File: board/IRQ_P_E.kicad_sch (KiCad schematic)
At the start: 21 parts, among them IC5 74LS219, IC6 74LS219, IC7 74LS219, IC8 74LS219, U13 74F08, U42 74F157, U43 74F157, U44 74LS148, U45 74LS148, U46 74F32

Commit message: Board V1.1G
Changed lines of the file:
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@@
 (kicad_sch
-	(version 20231120)
+	(version 20250114)
 	(generator "eeschema")
-	(generator_version "8.0")
+	(generator_version "9.0")
 	(paper "USLetter")
 	(title_block
 		(title "IRQ Priority Logic and Vector Memory")
 		(date "2025-03-04")
-		(rev "1.0F")
+		(rev "1.1A")
 		(company "Data Tuning")
 		(comment 1 "Hydra 16")
@@
 	(wire
 		(pts
-			(xy 181.61 33.02) (xy 195.58 33.02)
-		)
-		(stroke
-			(width 0)
-			(type default)
-		)
-	)
-	(wire
-		(pts
 			(xy 38.1 36.83) (xy 39.37 36.83)
 		)
@@
 	(wire
 		(pts
+			(xy 190.5 60.96) (xy 198.12 60.96)
+		)
+		(stroke
+			(width 0)
+			(type default)
+		)
+	)
+	(wire
+		(pts
 			(xy 36.83 153.67) (xy 36.83 175.26)
 		)
@@
 	(wire
 		(pts
-			(xy 195.58 33.02) (xy 195.58 60.96)
-		)
-		(stroke
-			(width 0)
-			(type default)
-		)
-	)
-	(wire
-		(pts
 			(xy 243.84 123.19) (xy 241.3 123.19)
 		)
@@
 	(wire
 		(pts
+			(xy 190.5 33.02) (xy 190.5 60.96)
+		)
+		(stroke
+			(width 0)
+			(type default)
+		)
+	)
+	(wire
+		(pts
 			(xy 191.77 118.11) (xy 186.69 118.11)
 		)
@@
 	(wire
 		(pts
-			(xy 153.67 27.94) (xy 184.15 27.94)
+			(xy 153.67 22.86) (xy 203.2 22.86)
 		)
 		(stroke
@@
 		)
 	)
+	(wire
+		(pts
+			(xy 181.61 33.02) (xy 190.5 33.02)
+		)
+		(stroke
+			(width 0)
+			(type default)
+		)
+	)
 	(bus
 		(pts
@@
 	(wire
 		(pts
+			(xy 153.67 22.86) (xy 153.67 27.94)
+		)
+		(stroke
+			(width 0)
+			(type default)
+		)
+	)
+	(wire
+		(pts
 			(xy 118.11 34.29) (xy 123.19 34.29)
 		)
@@
 	(wire
 		(pts
-			(xy 195.58 60.96) (xy 198.12 60.96)
-		)
-		(stroke
-			(width 0)
-			(type default)
-		)
-	)
-	(wire
-		(pts
 			(xy 227.33 135.89) (xy 227.33 165.1)
 		)
@@
 	(label "D3"
 		(at 76.2 139.7 0)
-		(fields_autoplaced yes)
 		(effects
 			(font
@@
 	(label "D7"
 		(at 77.47 157.48 0)
-		(fields_autoplaced yes)
 		(effects
 			(font
@@
 	(label "D2"
 		(at 77.47 144.78 0)
-		(fields_autoplaced yes)
 		(effects
 			(font
@@
 	(label "D3"
 		(at 151.13 139.7 0)
-		(fields_autoplaced yes)
 		(effects
 			(font
@@
 	(label "D5"
 		(at 36.83 157.48 0)
-		(fields_autoplaced yes)
 		(effects
 			(font
@@
 	(label "D4"
 		(at 101.6 157.48 0)
-		(fields_autoplaced yes)
 		(effects
 			(font
@@
 	(label "V3"
 		(at 195.58 104.14 0)
-		(fields_autoplaced yes)
 		(effects
 			(font
@@
 	(label "D7"
 		(at 152.4 157.48 0)
-		(fields_autoplaced yes)
 		(effects
 			(font
@@
 	(label "V0"
 		(at 195.58 73.66 0)
-		(fields_autoplaced yes)
 		(effects
 			(font
@@
 	(label "V1"
 		(at 195.58 83.82 0)
-		(fields_autoplaced yes)
 		(effects
 			(font
@@
 	(label "D1"
 		(at 106.68 142.24 0)
-		(fields_autoplaced yes)
 		(effects
 			(font
@@
 	(label "D0"
 		(at 36.83 137.16 0)
-		(fields_autoplaced yes)
 		(effects
 			(font
@@
 	(label "D4"
 		(at 33.02 157.48 0)
-		(fields_autoplaced yes)
 		(effects
 			(font
@@
 	(label "D6"
 		(at 148.59 157.48 0)
-		(fields_autoplaced yes)
 		(effects
 			(font
@@
 	(label "D5"
 		(at 105.41 157.48 0)
-		(fields_autoplaced yes)
 		(effects
 			(font
@@
 	(label "D0"
 		(at 105.41 137.16 0)
-		(fields_autoplaced yes)
 		(effects
 			(font
@@
 	(label "V2"
 		(at 195.58 93.98 0)
-		(fields_autoplaced yes)
 		(effects
 			(font
@@
 	(label "D6"
 		(at 73.66 157.48 0)
-		(fields_autoplaced yes)
 		(effects
 			(font
@@
 	(label "D1"
 		(at 38.1 142.24 0)
-		(fields_autoplaced yes)
 		(effects
 			(font
@@
 	(label "D2"
 		(at 152.4 144.78 0)
-		(fields_autoplaced yes)
 		(effects
 			(font
@@
 	(global_label "IRQB"
 		(shape output)
-		(at 184.15 27.94 0)
+		(at 203.2 22.86 0)
 		(fields_autoplaced yes)
 		(effects
@@
 		)
 		(property "Intersheetrefs" "${INTERSHEET_REFS}"
-			(at 191.6105 27.94 0)
+			(at 210.6605 22.86 0)
 			(effects
 				(font
@@
 		(dnp no)
 		(property "Reference" "U46"
-			(at 173.99 24.13 0)
+			(at 174.752 25.146 0)
 			(effects
 				(font
@@
 		)
 		(property "Value" "74F32"
-			(at 173.99 26.67 0)
+			(at 174.752 27.686 0)
 			(effects
 				(font

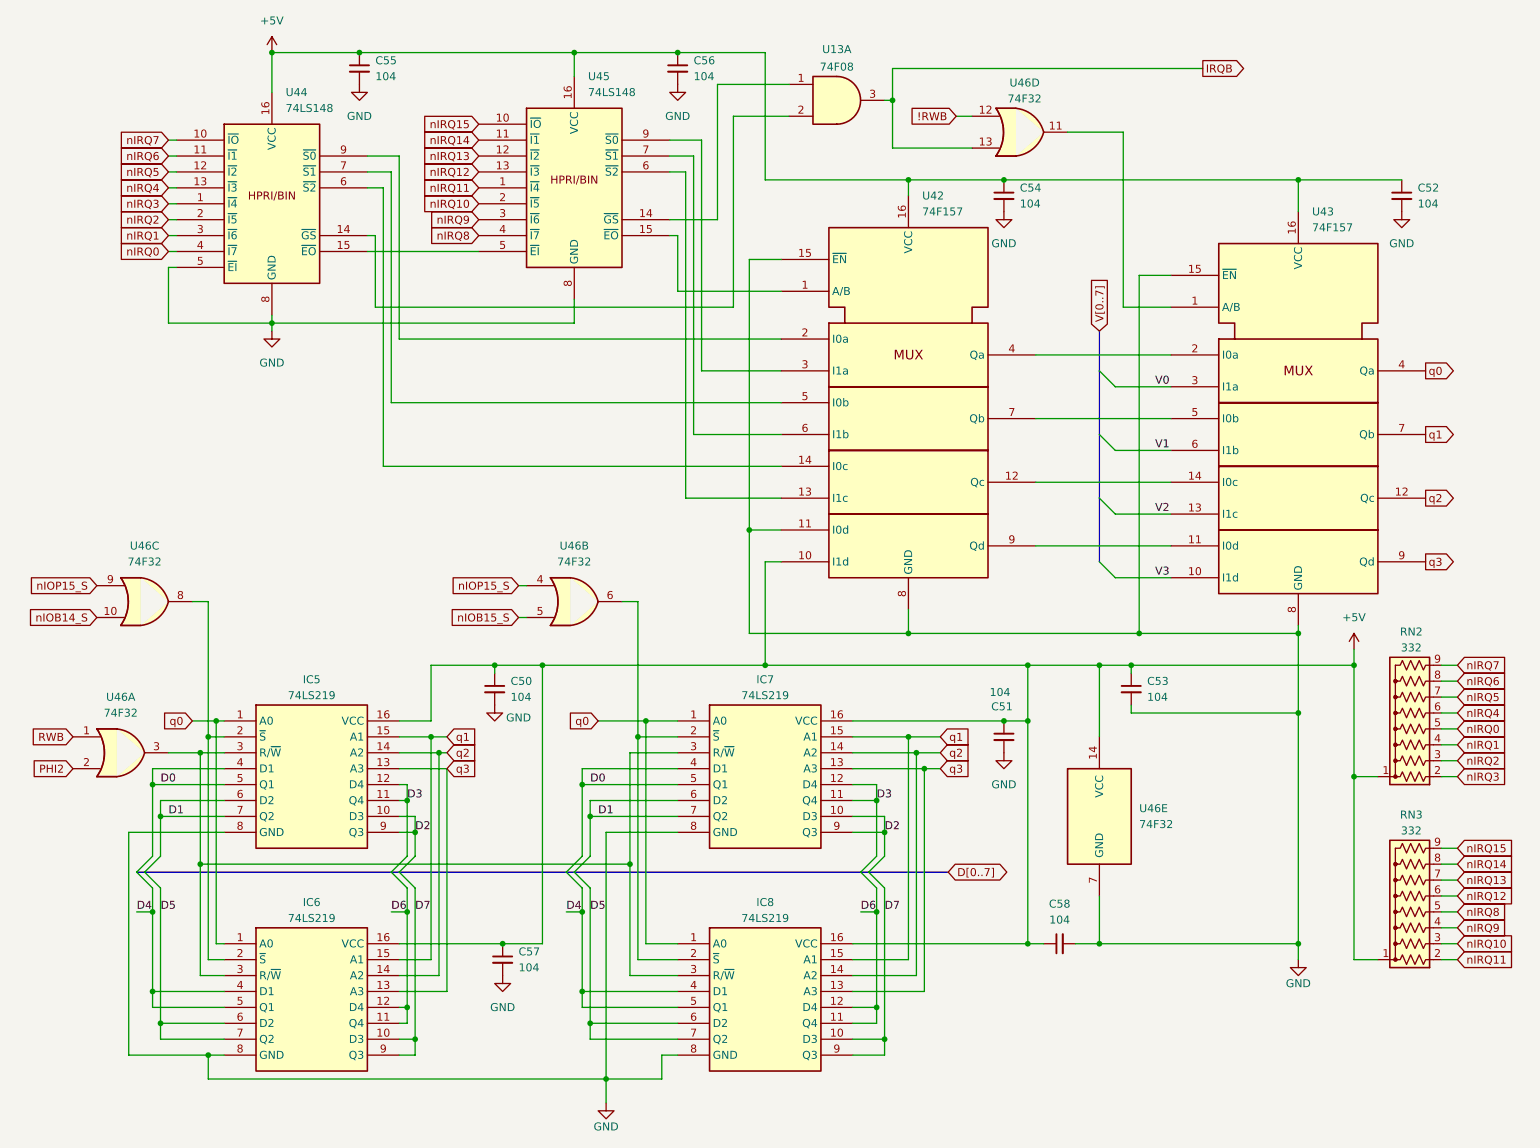
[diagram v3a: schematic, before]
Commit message: V1.3C without board traces
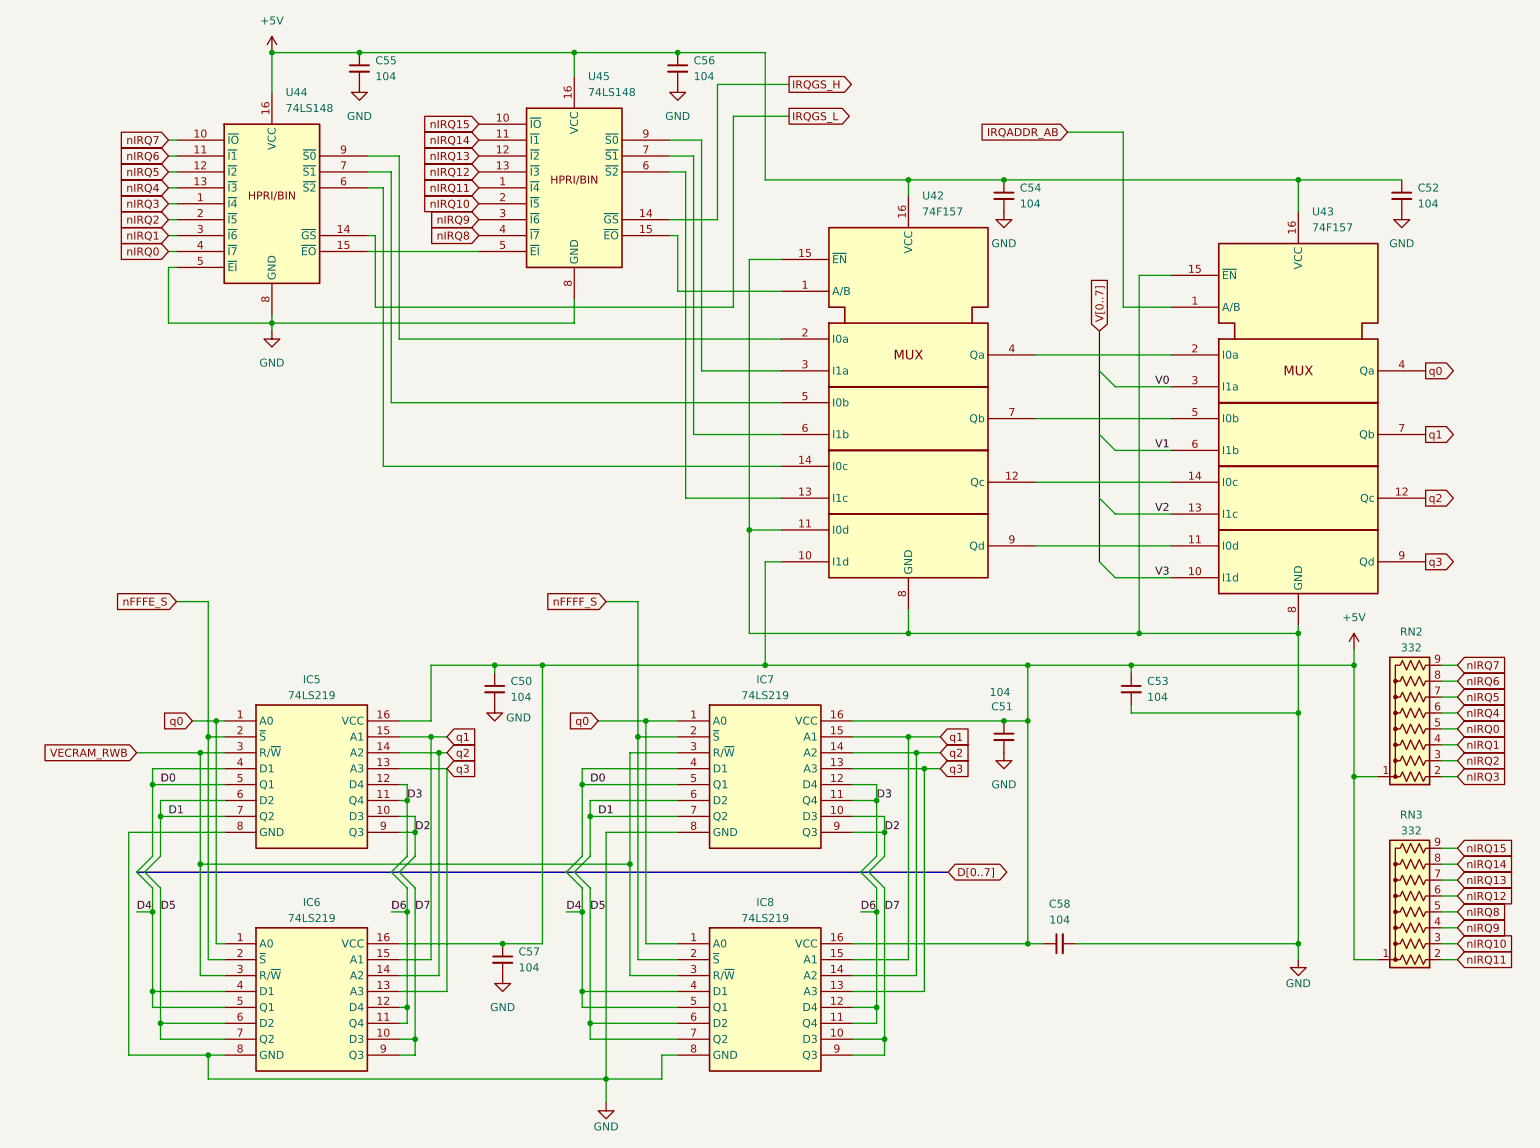
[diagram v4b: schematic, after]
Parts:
- removed U13: 74F08, Package_DIP:DIP-14_W7.62mm_Socket_LongPads, symbol 74xx:74LS08
- removed U46: 74F32, Package_DIP:DIP-14_W7.62mm_Socket_LongPads, symbol 74xx:74LS32
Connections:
- net IRQADDR_AB: now reaches U43.1 (A/B)
- net IRQGS_H: now reaches U45.14 (~{GS})
- net nFFFE_S: now reaches IC5.2 (~{S}), IC6.2 (~{S})
- net VECRAM_RWB: now reaches IC5.3 (R/~{W}), IC6.3 (R/~{W}), IC7.3 (R/~{W}), IC8.3 (R/~{W})
- net nFFFF_S: now reaches IC7.2 (~{S}), IC8.2 (~{S})
- net IRQGS_L: now reaches U44.14 (~{GS})

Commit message: Version 1.7A: More rearrangement, partial wiring of PDB, addition of W register
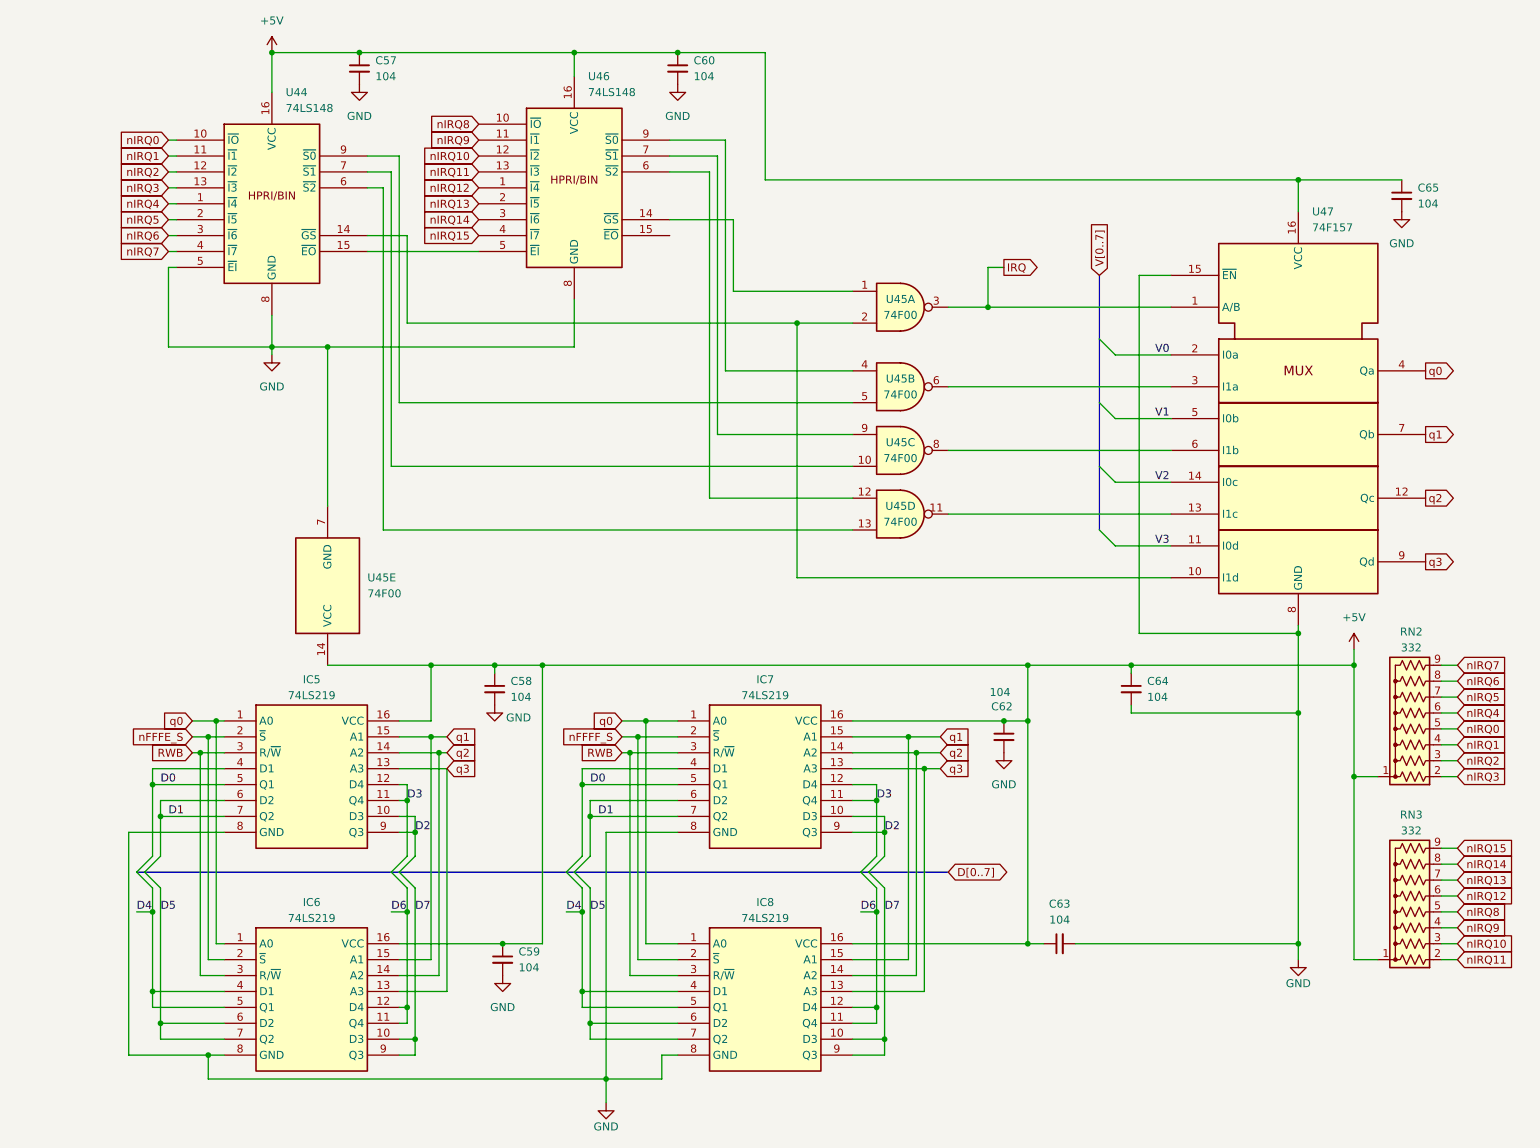
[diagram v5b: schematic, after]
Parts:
- removed C54: 104, Capacitor_THT:C_Disc_D5.0mm_W2.5mm_P5.00mm, symbol Device:C_Small
- added unit 2 of U45
- added unit 5 of U45
- added unit 1 of U45
- added unit 4 of U45
- U45: renamed from U42; value 74F157 -> 74F00; footprint Package_DIP:DIP-16_W7.62mm_Socket_LongPads -> Package_DIP:DIP-14_W7.62mm_Socket_LongPads; symbol 74xx_IEEE:74157 -> 74xx:74LS00
- renumbered C55 to C57, C50 to C58, C57 to C59, C56 to C60, C51 to C62, C58 to C63, C53 to C64, C52 to C65, U45 to U46, U43 to U47
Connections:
- net +5V: now also U45.14 (VCC); no longer U45.10 (I1d), U45.16 (VCC)
- net GND: now also U45.7 (GND); no longer U45.11 (I0d), U45.15 (~{EN}), U45.8 (GND)
- net V0: now also U47.2 (I0a); no longer U47.3 (I1a)
- net V1: now also U47.5 (I0b); no longer U47.6 (I1b)
- net V2: now also U47.14 (I0c); no longer U47.13 (I1c)
- net V3: now also U47.11 (I0d); no longer U47.10 (I1d)
- net nIRQ0: now also U44.10 (~{IO}); no longer U44.4 (~{I7})
- net nIRQ1: now also U44.11 (~{I1}); no longer U44.3 (~{I6})
- net nIRQ10: now also U46.12 (~{I2}); no longer U46.2 (~{I5})
- net nIRQ11: now also U46.13 (~{I3}); no longer U46.1 (~{I4})
- net nIRQ12: now also U46.1 (~{I4}); no longer U46.13 (~{I3})
- net nIRQ13: now also U46.2 (~{I5}); no longer U46.12 (~{I2})
- net nIRQ14: now also U46.3 (~{I6}); no longer U46.11 (~{I1})
- net nIRQ15: now also U46.4 (~{I7}); no longer U46.10 (~{IO})
- net nIRQ2: now also U44.12 (~{I2}); no longer U44.2 (~{I5})
- net nIRQ3: now also U44.13 (~{I3}); no longer U44.1 (~{I4})
- net nIRQ4: now also U44.1 (~{I4}); no longer U44.13 (~{I3})
- net nIRQ5: now also U44.2 (~{I5}); no longer U44.12 (~{I2})
- net nIRQ6: now also U44.3 (~{I6}); no longer U44.11 (~{I1})
- net nIRQ7: now also U44.4 (~{I7}); no longer U44.10 (~{IO})
- net nIRQ8: now also U46.10 (~{IO}); no longer U46.4 (~{I7})
- net nIRQ9: now also U46.11 (~{I1}); no longer U46.3 (~{I6})
- net at U46.15 (~{EO}): no longer U45.1 (A/B)
- net at U46.6 (~{S2}): now also U45.12; no longer U45.13 (I1c)
- net at U44.6 (~{S2}): now also U45.13; no longer U45.14 (I0c)
- net at U44.9 (~{S0}): now also U45.5; no longer U45.2 (I0a)
- net at U46.9 (~{S0}): now also U45.4; no longer U45.3 (I1a)
- net at U44.7 (~{S1}): now also U45.10; no longer U45.5 (I0b)
- net at U46.7 (~{S1}): now also U45.9; no longer U45.6 (I1b)
- net IRQADDR_AB renamed IRQ
- net IRQ: now also U45.3
- net IRQGS_H: no longer names the net of U46.14 (~{GS})
- net IRQGS_H: now also U45.1
- net IRQGS_L: no longer names the net of U44.14 (~{GS})
- net IRQGS_L: now also U47.10 (I1d), U45.2
- net VECRAM_RWB renamed RWB
- new net: U45.6, U47.3 (I1a)
- new net: U45.8, U47.6 (I1b)
- new net: U45.11, U47.13 (I1c)
